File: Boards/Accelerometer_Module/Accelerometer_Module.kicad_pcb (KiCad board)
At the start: 2 copper layers, 109.3 x 58.3 mm, 19 parts, among them U101 TPS560430YF

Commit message: Initial Board Layout
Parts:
- removed G***: LOGO, footprints:Logo_Large
- removed G***: LOGO, footprints:phoenix
- added C1: C_100nF, footprints:C_0603_1608Metric, F.Cu at (86.4, 117.2)
- added C2: C_10uF, footprints:C_0805_OEM, B.Cu at (68.1, 115.7)
- added C3: C_0.1uF, footprints:C_0805_OEM, F.Cu at (60.1, 100.6)
- added C4: C_0.1uF, footprints:C_0805_OEM, B.Cu at (68.1, 119.1)
- added C5: C_10uF, footprints:C_0805_OEM, F.Cu at (53.3, 135.4)
- added C6: C_1uF, footprints:C_0805_OEM, F.Cu at (55.2, 135.4)
- added C7: C_0.1uF, footprints:C_0805_OEM, F.Cu at (57.0, 135.4)
- added D1: LED_0805_Red, footprints:LED_0805_OEM, F.Cu at (74.4, 144.8)
- added D2: LED_0805_Red, footprints:LED_0805_OEM, F.Cu at (82.3, 123.1)
- added D3: LED_0805, footprints:LED_0805_OEM, F.Cu at (70.3, 144.8)
- added D4: LED_0805_Red, footprints:LED_0805_OEM, F.Cu at (78.3, 123.1)
- added D5: LED_0805, footprints:LED_0805_OEM, F.Cu at (78.5, 144.8)
- added D6: LED_0805, footprints:LED_0805_OEM, F.Cu at (82.6, 144.8)
- added D7: LED_0805, footprints:LED_0805_OEM, F.Cu at (86.7, 144.8)
- added DNP1: Crystal_SMD, footprints:Crystal_SMD_FA238, F.Cu at (83.4, 118.6)
- added DNP2: C_30pF, footprints:C_0805_OEM, F.Cu at (83.3, 116.0)
- added DNP3: C_30pF, footprints:C_0805_OEM, F.Cu at (80.4, 118.3)
- added J1: CONN_02X03, footprints:Pin_Header_Straight_2x03, F.Cu at (78.4, 134.9)
- added J2: SD_socket, footprints:sd_socket_molex_5009980900, F.Cu at (58.8, 118.5)
- added R1: R_200, footprints:R_0805_OEM, F.Cu at (74.3, 141.5)
- added R10: R_10K, footprints:R_0805_OEM, F.Cu at (101.4, 118.1)
- added R11: R_10K, footprints:R_0805_OEM, F.Cu at (60.3, 140.5)
- added R12: R_200, footprints:R_0805_OEM, F.Cu at (78.6, 141.5)
- added R13: R_200, footprints:R_0805_OEM, F.Cu at (82.6, 141.5)
- added R14: R_200, footprints:R_0805_OEM, F.Cu at (86.6, 141.5)
- added R2: R_200, footprints:R_0805_OEM, F.Cu at (83.3, 125.0)
- added R3: R_10K, footprints:R_0805_OEM, F.Cu at (99.0, 110.7)
- added R4: R_200, footprints:R_0805_OEM, F.Cu at (70.4, 141.5)
- added R5: R_200, footprints:R_0805_OEM, F.Cu at (79.9, 125.0)
- added R6: R_10K, footprints:R_0805_OEM, F.Cu at (61.1, 134.7)
- added R7: R_10K, footprints:R_0805_OEM, F.Cu at (46.5, 101.9)
- added R8: R_10K, footprints:R_0805_OEM, F.Cu at (101.4, 114.3)
- added R9: R_10K, footprints:R_0805_OEM, F.Cu at (101.4, 116.2)
- added SW1: SW_Push_SPST_NO, footprints:SW_B3U-1000P_4.2x1.7mm, F.Cu at (62.7, 144.0)
- added U1: ATmega328P-AU, Package_QFP:TQFP-32_7x7mm_P0.8mm, F.Cu at (91.0, 122.5)
- added U2: LIS3DHTR, footprints:LIS3DHTR, B.Cu at (72.6, 117.9)
- added U3: INA260, Package_SO:TSSOP-16_4.4x5mm_P0.65mm, F.Cu at (54.2, 98.1)
- C102: value C_2.2uF -> C_4.7uF
- L101: value L_100uH -> L_15uH; footprint footprints:L_100uH -> footprints:L_100uH_OEM
- R103: value R_100K -> R_54.9K
- moved L101 48.9 mm to (81.2, 98.2)
- moved R103 48.8 mm to (81.1, 91.4), turned to 0 degrees
- moved R101 48.8 mm to (63.6, 95.9)
- moved R104 48.8 mm to (78.9, 102.1)
- moved C101 48.8 mm to (73.5, 94.4)
- moved C103 48.8 mm to (81.7, 94.5)
- moved COUT101 48.8 mm to (85.7, 95.8)
- moved D101 48.8 mm to (68.7, 96.2)
- moved D102 48.8 mm to (63.6, 92.1)
- moved F101 48.8 mm to (73.7, 98.2)
- moved R102 48.8 mm to (77.2, 91.5)
- moved R105 48.8 mm to (77.4, 105.9)
- moved U101 48.8 mm to (78.4, 94.5)
- moved COUT102 48.8 mm to (84.6, 102.1)
- moved COUT103 48.8 mm to (85.7, 98.1)
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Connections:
- net /12V renamed /9V
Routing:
- net /Protect: track 0.00 -> 69.5 mm, vias 0 -> 6
- net /SCL: track 0.00 -> 63.0 mm, vias 0 -> 4
- net /ALERT: track 0.00 -> 62.0 mm
- net /SDA: track 0.00 -> 61.8 mm, vias 0 -> 2
- net /Detect: track 0.00 -> 57.7 mm
- net /SCK: track 0.00 -> 52.6 mm, vias 0 -> 5
- net /MISO: track 0.00 -> 50.4 mm, vias 0 -> 2
- net /MOSI: track 0.00 -> 47.3 mm, vias 0 -> 2
- net Net-(SW1-Pad1): track 0.00 -> 41.1 mm, vias 0 -> 4
- net /CS_SD: track 0.00 -> 39.8 mm
- net Net-(R4-Pad1): track 0.00 -> 28.8 mm, vias 0 -> 2
- net Net-(R1-Pad1): track 0.00 -> 27.4 mm, vias 0 -> 2
- net /PC2: track 0.00 -> 25.7 mm
- net /PC0: track 0.00 -> 24.8 mm
- net /CS: track 0.00 -> 24.7 mm, vias 0 -> 3
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- removed copper zone on B.Cu, net GND
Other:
- board size 109.3 x 58.3 mm -> 66.2 x 66.2 mm
- board text added: "9V"
- board text removed: "12V"

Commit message: Editing Layout
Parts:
- moved D2 22.5 mm to (72.3, 143.3), turned to 270 degrees
- moved D4 22.1 mm to (69.5, 143.3), turned to 270 degrees
- moved J1 22.1 mm to (98.0, 124.8), turned to 180 degrees
- moved R2 18.0 mm to (72.3, 139.3), turned to 90 degrees
- moved R5 17.8 mm to (69.5, 139.3), turned to 270 degrees
- moved C2 9.00 mm to (76.5, 119.0), turned to 90 degrees
- moved R10 7.08 mm to (94.6, 116.3)
- moved R8 7.08 mm to (94.6, 112.5)
- moved R9 7.08 mm to (94.5, 114.4)
- moved DNP2 6.17 mm to (78.1, 112.6)
- moved C1 6.15 mm to (81.8, 113.1)
- moved DNP1 6.13 mm to (78.3, 115.2)
- moved U1 6.01 mm to (85.9, 119.2)
- moved DNP3 5.81 mm to (75.4, 115.4)
- moved C4 5.57 mm to (71.2, 114.6), turned to 180 degrees
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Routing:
- net /RESET: track 11.4 -> 22.6 mm, vias 2 -> 3
- net /SCL: track 63.0 -> 53.2 mm
- net /ALERT: track 62.0 -> 52.8 mm
- net /CS_SD: track 39.8 -> 48.7 mm, vias 0 -> 2
- net Net-(R1-Pad1): track 27.4 -> 18.5 mm
- net Net-(SW1-Pad1): track 41.1 -> 32.4 mm
- net Net-(R4-Pad1): track 28.8 -> 20.3 mm
- net /SDA: track 61.8 -> 53.4 mm
- net /CS: track 24.7 -> 33.1 mm
- net VCC: track 41.4 -> 49.8 mm
- net GND: track 70.0 -> 76.6 mm
- net /PC2: track 25.7 -> 21.8 mm
- net /SCK: track 52.6 -> 56.4 mm, vias 5 -> 3
- net /Detect: track 57.7 -> 54.2 mm, vias 0 -> 4
- net Net-(D5-Pad2): track 3.40 -> 0.00 mm
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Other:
- board text added: "3.3V"
- board text removed: "5V"

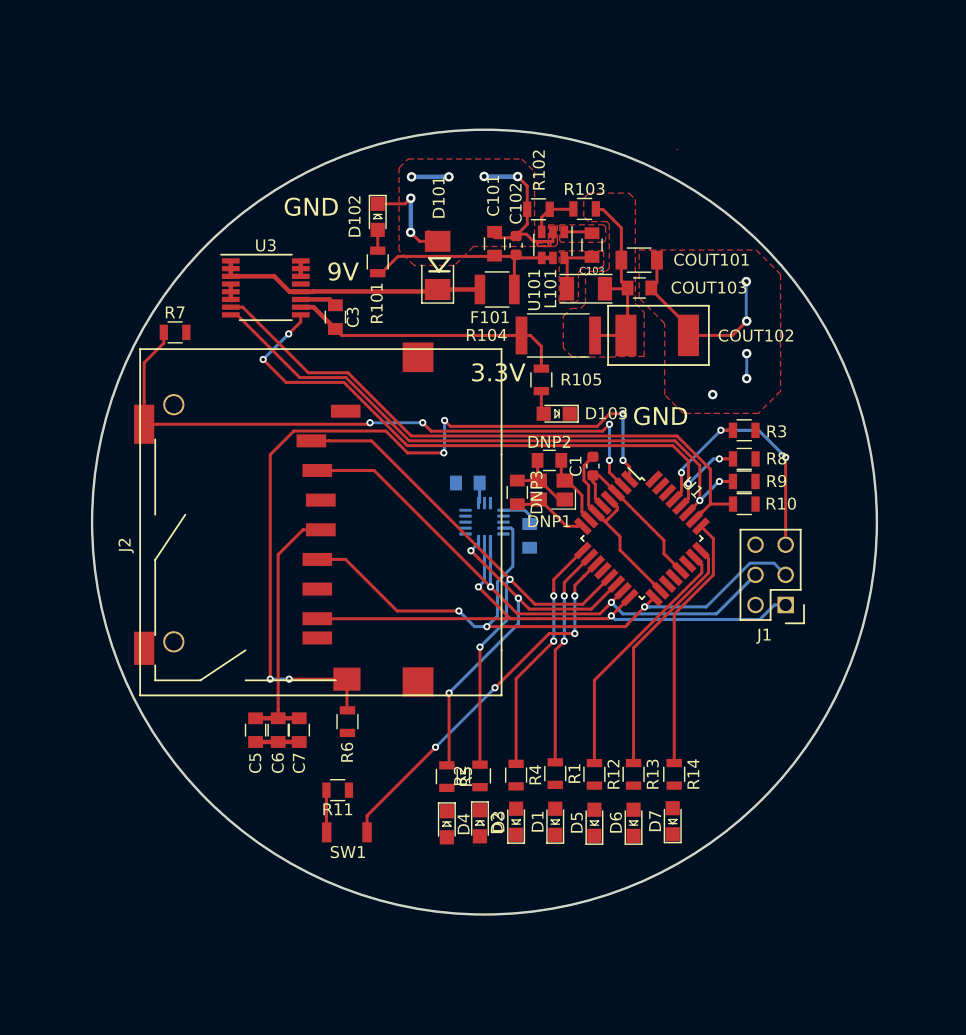
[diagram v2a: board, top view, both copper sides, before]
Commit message: Added Ground Plane
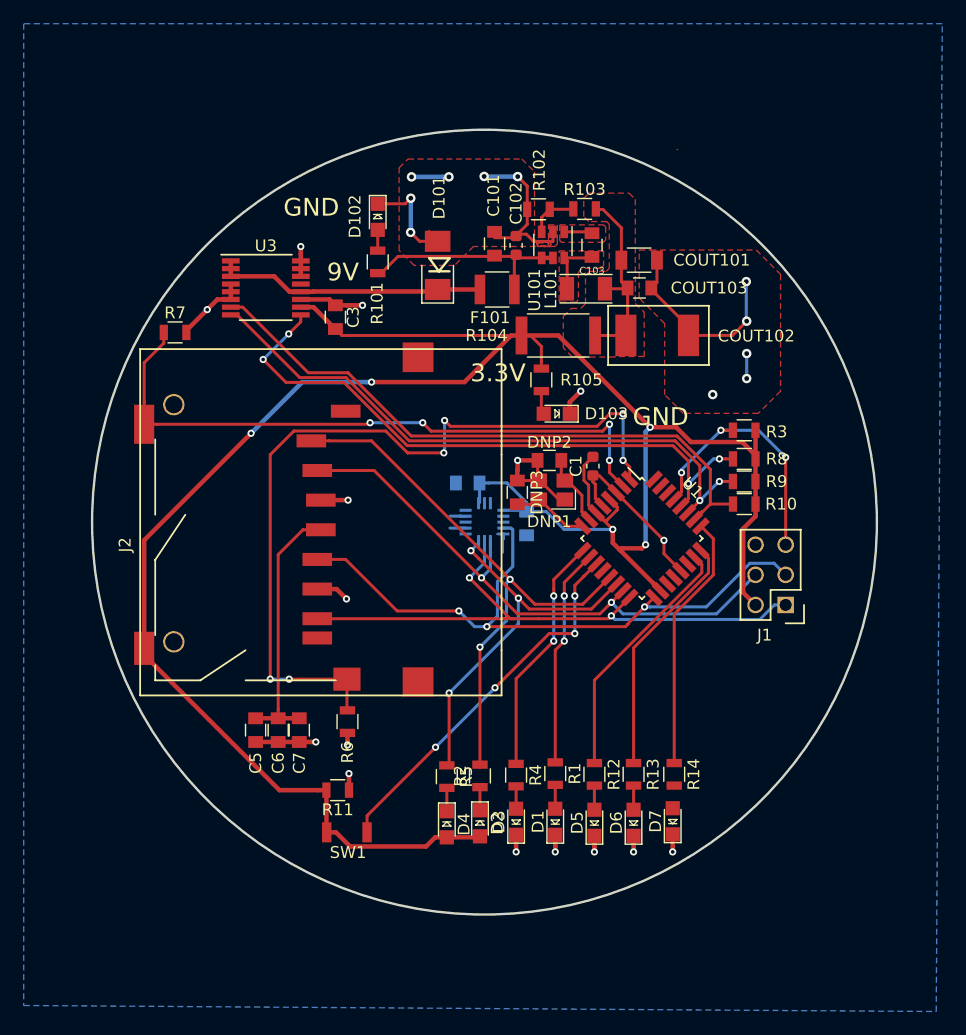
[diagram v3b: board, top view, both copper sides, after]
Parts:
- moved C2 1.08 mm to (76.2, 118.0)
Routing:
- net VCC: track 49.8 -> 197.0 mm, vias 0 -> 5
- net GND: track 76.6 -> 111.5 mm, vias 11 -> 27
- net Net-(D6-Pad2): track 0.00 -> 2.04 mm
- net Net-(D5-Pad2): track 0.00 -> 2.04 mm
- net Net-(D1-Pad2): track 0.00 -> 2.01 mm
- net Net-(D4-Pad1): track 0.00 -> 1.97 mm
- net Net-(D2-Pad1): track 0.00 -> 1.95 mm
- net Net-(D3-Pad2): track 0.00 -> 1.89 mm
- net /MISO: track 50.7 -> 51.4 mm
- added copper zone on B.Cu, net GND

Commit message: Final Schamtic and Layout
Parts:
- added G***: LOGO, footprints:Logo_Large, B.Cu at (72.4, 132.7)
- C5, C6, C7: moved to B.Cu
- R1, R105, R12, R13, R14, R2, R4, R5: value R_200 -> R_100
- R101: value R_200 -> R_499
- moved R7 39.6 mm to (76.3, 127.9), turned to 45 degrees
- moved R6 34.2 mm to (50.6, 102.1), turned to 180 degrees
- moved C7 20.0 mm to (54.2, 115.6), turned to 180 degrees
- moved C6 18.1 mm to (54.2, 117.3), turned to 180 degrees
- moved C5 16.2 mm to (54.2, 119.3), turned to 180 degrees
- moved D5 6.08 mm to (88.0, 142.6), turned to 180 degrees
- moved D7 4.56 mm to (88.0, 138.6), turned to 180 degrees
- moved R14 4.55 mm to (84.1, 138.6), turned to 0 degrees
- moved R11 4.54 mm to (62.3, 136.4)
- moved R12 4.14 mm to (84.1, 142.6), turned to 0 degrees
- moved D6 3.80 mm to (88.0, 140.6), turned to 180 degrees
- moved R13 1.82 mm to (84.1, 140.6), turned to 0 degrees
- moved R5 1.40 mm to (68.1, 139.3)
- moved D4 1.40 mm to (68.1, 143.3)
- moved J2 1.13 mm to (58.9, 117.4), turned to 90 degrees
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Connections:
- C5 pad 1: Net-(C5-Pad1) -> VCC
- C6 pad 1: Net-(C5-Pad1) -> VCC
- C7 pad 1: Net-(C5-Pad1) -> VCC
- J2 pad 4: Net-(C5-Pad1) -> VCC
- R11 pad 1: GND -> Net-(R11-Pad1)
- R11 pad 2: VCC -> GND
- R4 pad 1: Net-(R4-Pad1) -> Net-(D3-Pad2)
- R4 pad 2: Net-(D3-Pad2) -> Net-(R4-Pad2)
- SW1 pad 1: Net-(SW1-Pad1) -> Net-(R11-Pad1)
- U1 pad 11: Net-(SW1-Pad1) -> Net-(R11-Pad1)
- U1 pad 9: Net-(R4-Pad1) -> Net-(R4-Pad2)
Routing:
- net Net-(R11-Pad1): track 0.00 -> 37.9 mm, vias 0 -> 4
- net Net-(SW1-Pad1): track 32.4 -> 0.00 mm, vias 4 -> 0
- net /Protect: track 68.6 -> 42.9 mm, vias 6 -> 4
- net Net-(C5-Pad1): track 22.7 -> 0.00 mm
- net Net-(R4-Pad2): track 0.00 -> 20.7 mm, vias 0 -> 2
- net Net-(R4-Pad1): track 20.3 -> 0.00 mm, vias 2 -> 0
- net /SCK: track 56.4 -> 67.3 mm, vias 3 -> 4
- net /CS_SD: track 48.7 -> 40.3 mm
- net VCC: track 197.0 -> 204.5 mm, vias 5 -> 6
- net /PC0: track 21.4 -> 26.8 mm
- net /SCL: track 53.2 -> 48.0 mm
- net /MOSI: track 48.9 -> 44.3 mm, vias 2 -> 3
- net /PC1: track 20.8 -> 24.8 mm
- net /9V: track 23.0 -> 26.3 mm, vias 0 -> 1
- net /Detect: track 54.2 -> 51.2 mm, vias 4 -> 6
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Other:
- board text added: "Accelerometer"
- board text added: "Acceleromoeter"
- board text added: "Atmega328P"
- board text added: "Battery Level"
- board text added: "Battery Monitor"
- board text added: "HIGH"
- board text added: "LED Layout"
- board text added: "LOW"
- board text added: "Luke Nonas-Hunter 12/05/2019 Accelerometer Module V0"
- board text added: "MED"
- board text added: "ON"
- board text added: "PC0-"
- board text added: "PC1-"
- board text added: "PC2-"
- board text added: "PD5"
- board text added: "PD6"
- board text added: "Place Accelerometer as close to location of measurement as possible."
- board text added: "READY"
- board text added: "Record Data"
- board text added: "SD Card"

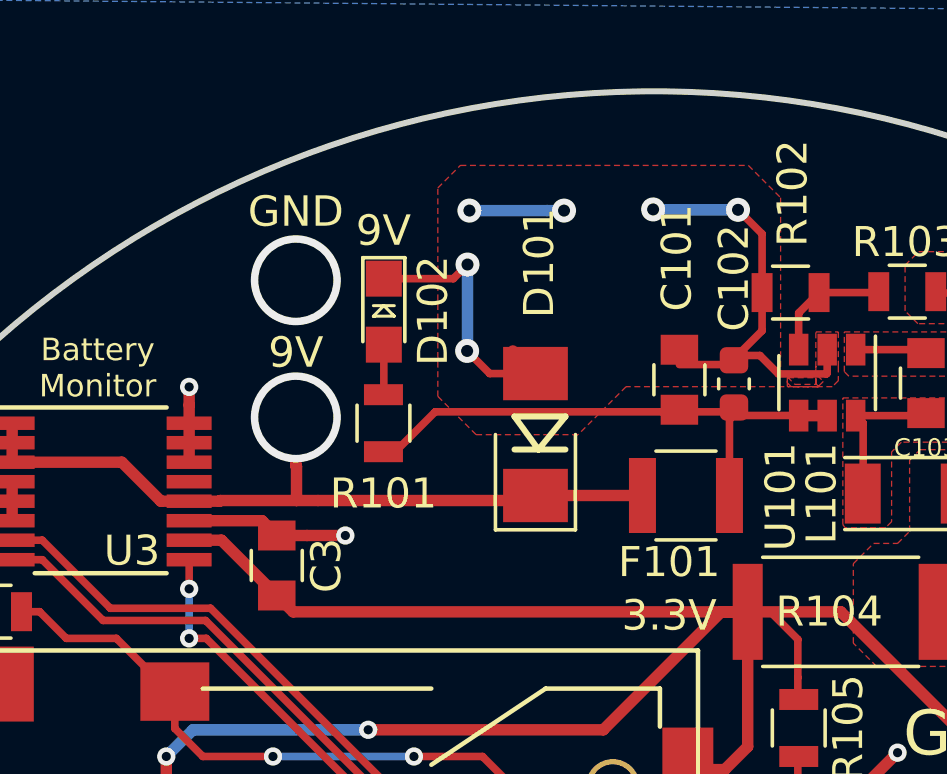
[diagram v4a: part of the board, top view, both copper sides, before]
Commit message: Fixing Layout to Account for Schematic Changes
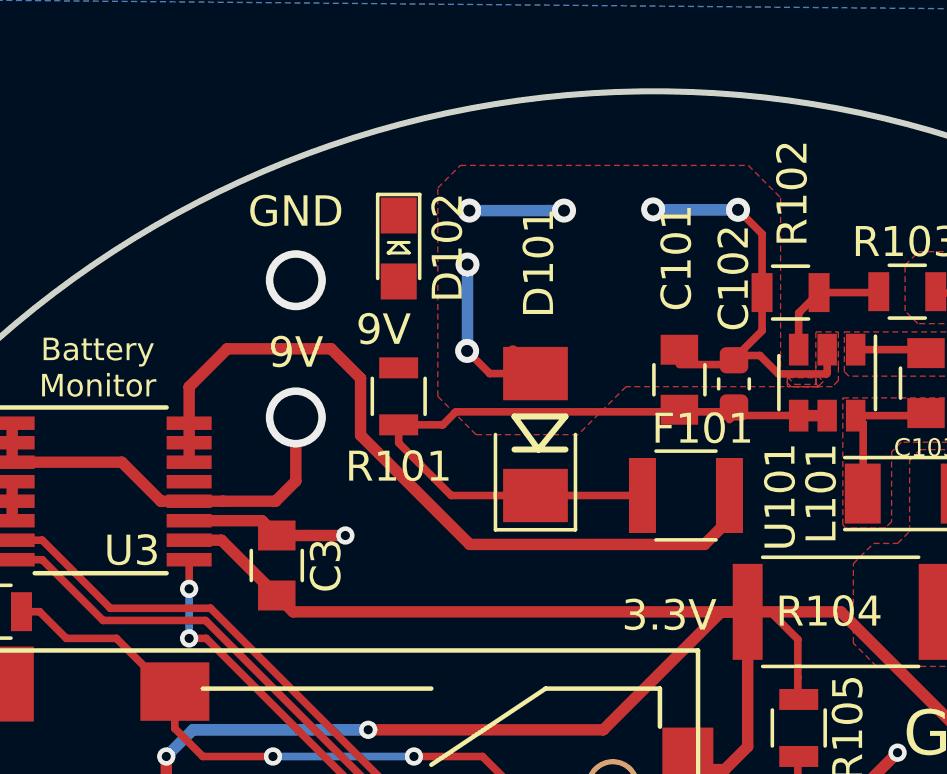
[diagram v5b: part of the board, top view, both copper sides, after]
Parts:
- moved D102 2.16 mm to (64.1, 90.0)
- moved R101 1.03 mm to (64.1, 94.9)
- turned F101 to 0 degrees
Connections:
- D101 pad 1: /9V -> Net-(C101-Pad1)
- F101 pad 2: /9V -> /9V_out
- U3 pad 1: /9V -> /9V_in
- U3 pad 12: /9V -> /9V_in
- U3 pad 14: GND -> /9V_out
- U3 pad 15: GND -> /9V_out
- U3 pad 16: GND -> /9V_out
- U3 pad 2: /9V -> /9V_in
- U3 pad 3: /9V -> /9V_in
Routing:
- net /9V: track 26.3 -> 0.00 mm, vias 1 -> 0
- net /9V_out: track 0.00 -> 26.0 mm
- net /9V_in: track 0.00 -> 13.7 mm, vias 0 -> 1
- net Net-(C101-Pad1): track 18.1 -> 24.5 mm
- net GND: track 111.8 -> 106.3 mm, vias 26 -> 25
- net Net-(D102-Pad2): track 1.75 -> 0.00 mm
